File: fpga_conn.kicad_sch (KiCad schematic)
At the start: 1 part, among them J3 Conn_02x25_Odd_Even

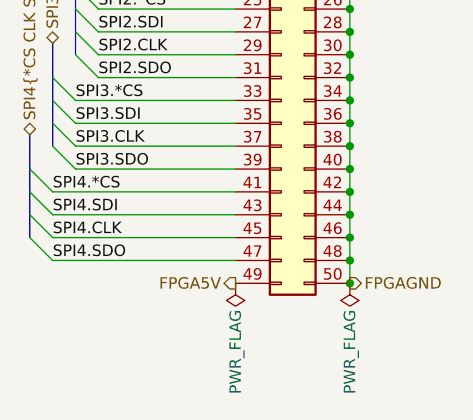
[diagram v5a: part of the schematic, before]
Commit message: remove 5V (now 3.3V) + tuning
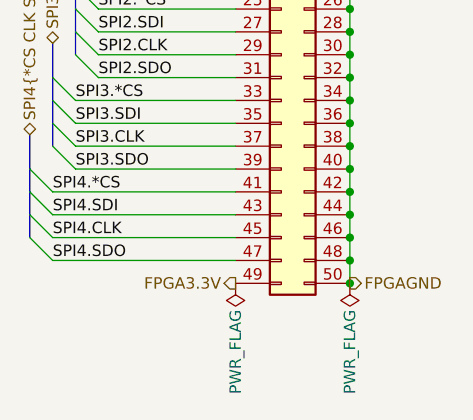
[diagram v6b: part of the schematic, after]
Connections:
- net FPGA5V renamed FPGA3.3V
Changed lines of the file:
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@@
     (effects (font (size 1.27 1.27)) (justify left))
   )
-  (hierarchical_label "FPGA5V" (shape output) (at 234.95 116.84 180)
+  (hierarchical_label "FPGA3.3V" (shape output) (at 234.95 116.84 180)
     (effects (font (size 1.27 1.27)) (justify right))
   )
